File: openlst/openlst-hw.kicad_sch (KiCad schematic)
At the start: 73 parts, among them J10 Conn_01x02, J2 CC Prog/Debug, J3 UART0, J4 SPI0, J5 Control Outputs, J6 ANT, J9 Conn_01x02, U2 CC1110, U4 FOX924 27MHz, U5 TLV803S, U6 PE4259, U8 SF2446E, U9 RFFM6406

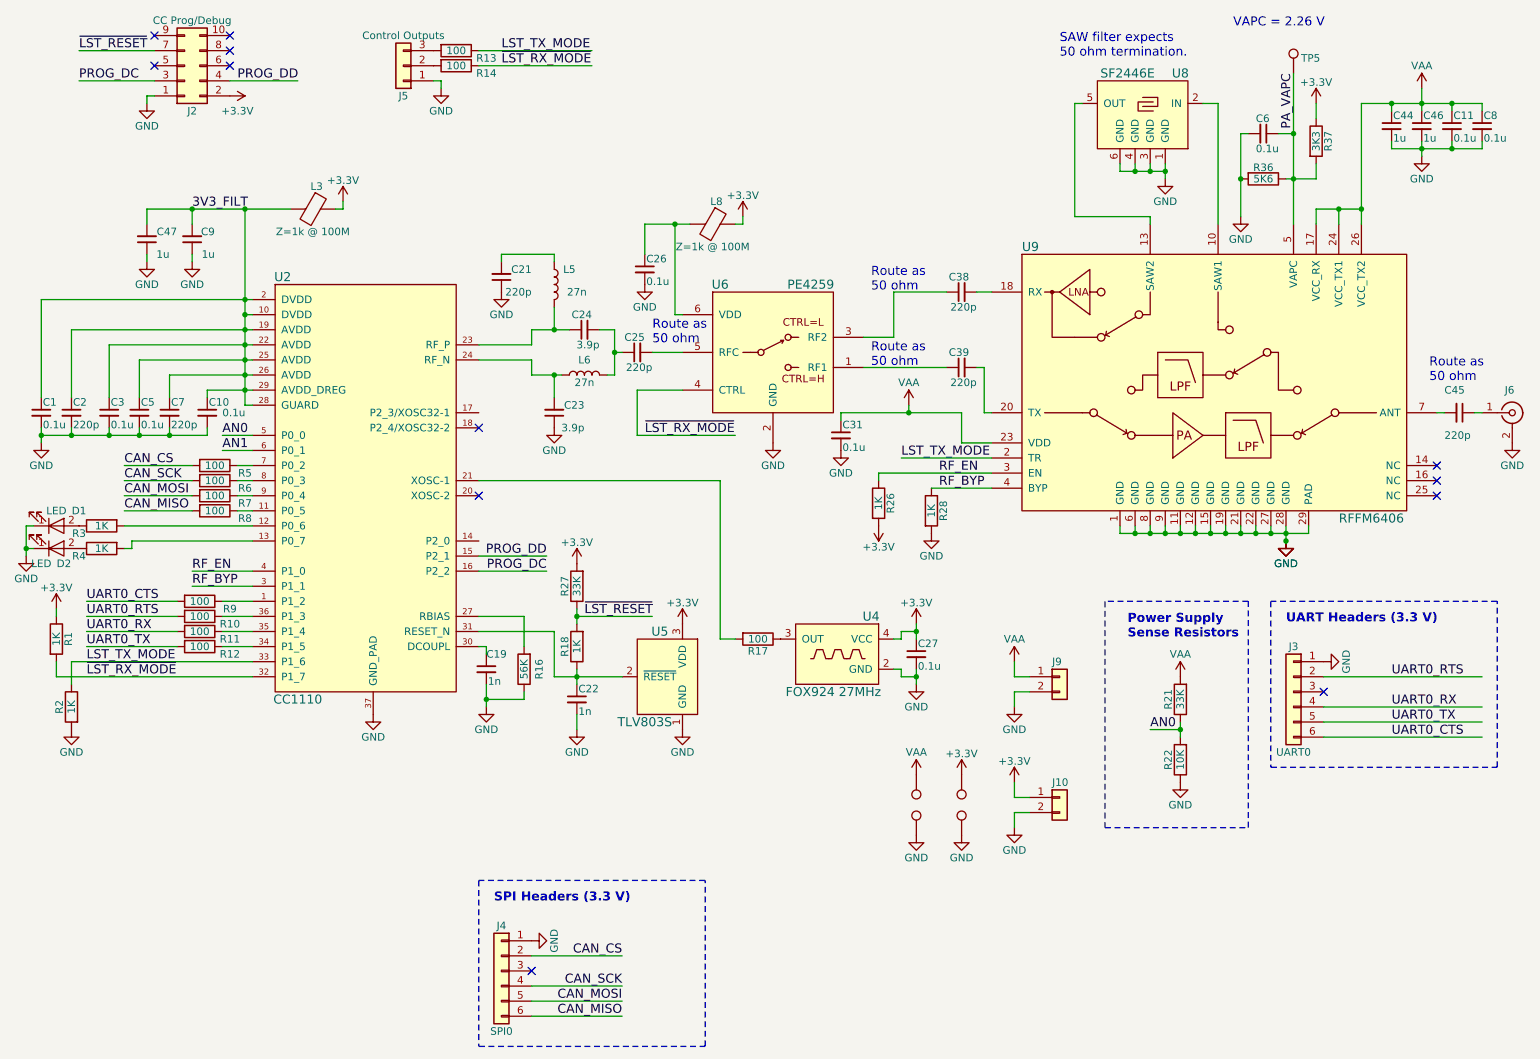
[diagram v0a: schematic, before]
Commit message: Finished schematic, partially finished BOM, cleaned up old files
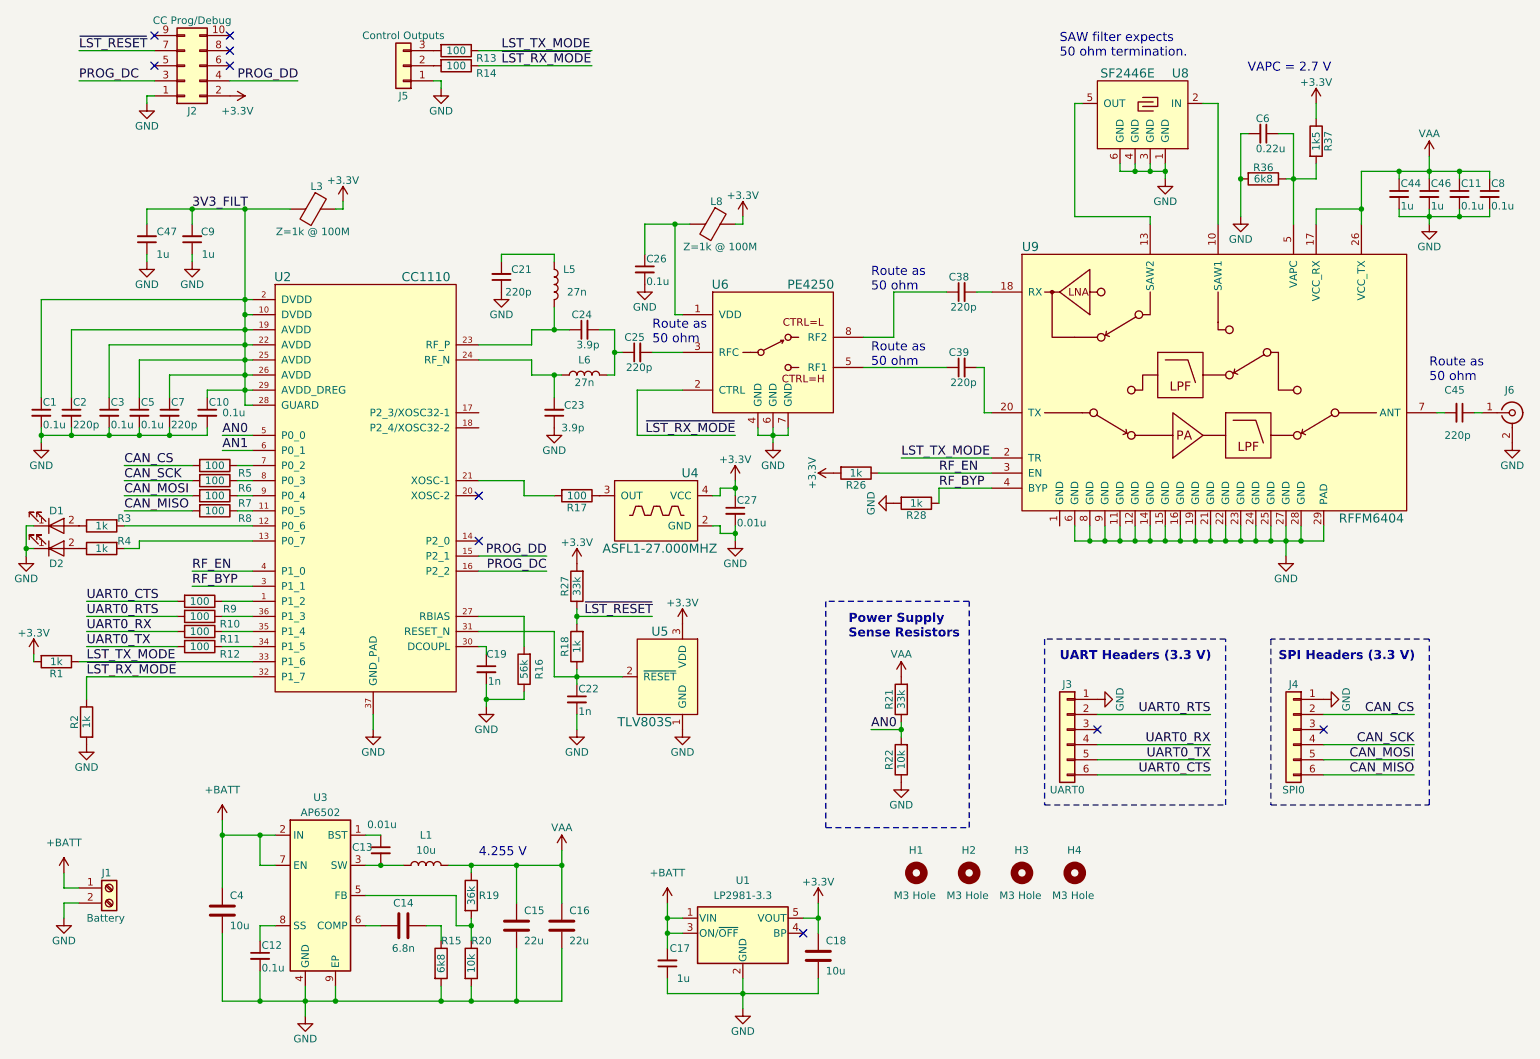
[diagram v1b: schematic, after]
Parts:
- removed C31: 0.1u, Capacitor_SMD:C_0603_1608Metric, symbol openlst-hw:C_Small
- removed J10, J9: Conn_01x02, Connector_PinHeader_2.54mm:PinHeader_1x02_P2.54mm_Vertical, symbol Connector_Generic:Conn_01x02
- removed TP1, TP2, TP3, TP4: TestPoint, TestPoint:TestPoint_Keystone_5010-5014_Multipurpose, symbol Connector:TestPoint
- removed TP5: TestPoint, TestPoint:TestPoint_Pad_D1.0mm, symbol Connector:TestPoint
- removed U6: PE4259, Package_TO_SOT_SMD:SOT-363_SC-70-6, symbol openlst-hw:PE4259
- removed U9: RFFM6406, openlst:Qorvo_LGA_28_ThermalVias, symbol openlst-hw:RFFM6406
- added C12: 0.1u, Capacitor_SMD:C_0603_1608Metric, symbol openlst-hw:C_Small
- added C13: 0.01u, Capacitor_SMD:C_0603_1608Metric, symbol openlst-hw:C_Small
- added C14: 6.8n, Capacitor_SMD:C_0603_1608Metric, symbol Device:C
- added C15, C16: 22u, symbol Device:C
- added C17: 1u, Capacitor_SMD:C_0603_1608Metric, symbol openlst-hw:C_Small
- added C18: 10u, Capacitor_SMD:C_0603_1608Metric, symbol Device:C
- added C4: 10u, Capacitor_SMD:C_0805_2012Metric, symbol Device:C
- added H1, H2, H3, H4: M3 Hole, MountingHole:MountingHole_3.2mm_M3, symbol Mechanical:MountingHole
- added J1: Battery, symbol Connector:Screw_Terminal_01x02
- added L1: 10u, Inductor_SMD:L_Vishay_IFSC-1515AH_4x4x1.8mm, symbol Device:L
- added R15: 6k8, Resistor_SMD:R_0603_1608Metric, symbol Device:R
- added R19: 36k, Resistor_SMD:R_0603_1608Metric, symbol Device:R
- added R20: 10k, Resistor_SMD:R_0603_1608Metric, symbol Device:R
- added U1: LP2981-3.3, Package_TO_SOT_SMD:SOT-23-5, symbol Regulator_Linear:LP2985-3.3
- added U3: AP6502, Package_SO:SOIC-8-1EP_3.9x4.9mm_P1.27mm_EP2.62x3.51mm_ThermalVias, symbol Regulator_Switching:AP6502
- added U6: PE4250, Package_SO:MSOP-8_3x3mm_P0.65mm, symbol openlst-hw:PE4250
- added U9: RFFM6404, openlst:Qorvo_LGA_28_ThermalVias, symbol openlst-hw:RFFM6404
- C1, C10, C11, C26, C3, C5, C8: Manuf AVX -> (none); ManufPN 0603YC104K4T4A -> (none); Supplier Digikey -> (none); SupplierPN 478-9382-1-ND -> (none)
- C19, C22: Manuf Murata -> (none); ManufPN GCM188R71E102KA37D -> (none); Supplier Digikey -> (none); SupplierPN 490-8016-1-ND -> (none)
- C2, C21, C25, C38, C39, C45, C7: Manuf Kemet -> (none); ManufPN C0402C221J2GACAUTO -> (none); Supplier Digikey -> (none); SupplierPN 399-11552-1-ND -> (none)
- C23, C24: Manuf Murata -> (none); ManufPN GJM1555C1H3R9CB01D -> (none); Supplier Digikey -> (none); SupplierPN 490-3097-1-ND -> (none)
- C27: value 0.1u -> 0.01u; Manuf AVX -> (none); ManufPN 0603YC104K4T4A -> (none); Supplier Digikey -> (none); SupplierPN 478-9382-1-ND -> (none)
- C44, C46, C47, C9: Manuf Samsung -> (none); ManufPN CL10B105MO8NNWC -> (none); Supplier Digikey -> (none); SupplierPN 1276-6524-6-ND -> (none)
- C6: value 0.1u -> 0.22u; Manuf AVX -> (none); ManufPN 0603YC104K4T4A -> (none); Supplier Digikey -> (none); SupplierPN 478-9382-1-ND -> (none)
- D1: Manuf Wurth -> (none); ManufPN 150060VS75000 -> (none); Supplier Digikey -> (none); SupplierPN 732-4980-1-ND -> (none)
- D2: Manuf Wurth -> (none); ManufPN 150060SS75000 -> (none); Supplier Digikey -> (none); SupplierPN 732-4979-1-ND -> (none)
- J2: Manuf Samtec -> (none); ManufPN FTSH-105-01-L-DV-K-P -> (none); Supplier Digikey -> (none); SupplierPN SAM9076-ND -> (none)
- J3, J4: Manuf Wurth -> (none); ManufPN 61300611121 -> (none); Supplier Digikey -> (none); SupplierPN 732-5319-ND -> (none)
- L3, L8: Manuf Wurth -> Pulse Electronics Network; ManufPN 74279266 -> PE-0603FB102ST; SupplierPN 732-4484-1-ND -> 553-2381-1-ND
- L5, L6: Manuf Murata -> (none); ManufPN LQW15AN27NJ00D -> (none); Supplier Digikey -> (none); SupplierPN 490-1151-1-ND -> (none)
- R1, R18, R2, R26, R28, R3, R4: value 1K -> 1k; Manuf Yageo -> (none); ManufPN RC0603JR-071KL -> (none); Supplier Digikey -> (none); SupplierPN 311-1.0KGRCT-ND -> (none)
- R10, R11, R12, R13, R14, R17, R5, R6, R7, R8, R9: Manuf Yageo -> (none); ManufPN AC0603FR-07100RL -> (none); Supplier Digikey -> (none); SupplierPN YAG3561CT-ND -> (none)
- R16: value 56K -> 56k; Manuf Stackpole -> (none); ManufPN RMCF0603FT56K0 -> (none); Supplier Digikey -> (none); SupplierPN RMCF0603FT56K0CT-ND -> (none)
- R21, R27: value 33K -> 33k; Manuf Yageo -> (none); ManufPN AC0603FR-0733KL -> (none); Supplier Digikey -> (none); SupplierPN YAG3598CT-ND -> (none)
- R22: value 10K -> 10k; Manuf Yageo -> (none); ManufPN RC0603JR-0710KL -> (none); Supplier Digikey -> (none); SupplierPN 311-10KGRCT-ND -> (none)
- R36: value 5K6 -> 6k8; Manuf Stackpole -> (none); ManufPN RMCF0603FT5K60 -> (none); Supplier Digikey -> (none); SupplierPN RMCF0603FT5K60CT-ND -> (none)
- R37: value 3K3 -> 1k5; Manuf Stackpole -> (none); ManufPN RMCF0603FT3K30 -> (none); Supplier Digikey -> (none); SupplierPN RMCF0603FT3K30CT-ND -> (none)
- U2: Supplier Digikey -> Texas Instruments; SupplierPN 296-38560-1-ND -> CC1110F32RHHR
- U4: value FOX924 27MHz -> ASFL1-27.000MHZ; footprint Oscillator:Oscillator_SMD_Fordahl_DFAS15-4Pin_5.0x3.2mm -> Oscillator:Oscillator_SMD_SeikoEpson_SG8002LB-4Pin_5.0x3.2mm; Manuf Fox Electronics -> Abracon; ManufPN FT5HNBPK27.0-T1 -> ASFL1-27.000MHZ-EK-T; SupplierPN 631-1075-1-ND -> 535-9263-1-ND
- U8: Manuf (none) -> RFMi; ManufPN (none) -> SF2446E; Supplier (none) -> Digikey Marketplace; SupplierPN (none) -> 2410-SF2446E-ND
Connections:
- net +3V3: now also R1.2, C18.1, U1.5 (VOUT); no longer R1.1
- net GND: now also C12.2, C15.2, C16.2, C17.1, C18.2, C4.1, J1.2 (Pin_2), R15.2, R20.2, U1.2 (GND), U3.4 (GND), U3.9 (EP), U6.4 (GND), U6.6 (GND), U6.7 (GND), U9.11 (GND), U9.12 (GND), U9.14 (GND), U9.15 (GND), U9.16 (GND), U9.19 (GND), U9.21 (GND), U9.22 (GND), U9.23 (GND), U9.24 (GND), U9.25 (GND), U9.27 (GND), U9.28 (GND), U9.29 (PAD), U9.6 (GND), U9.8 (GND), U9.9 (GND)
- net LST_TX_MODE: now also R1.1, U9.2 (TR); no longer R2.1
- net RF_BYP: now also U9.4 (BYP)
- net RF_EN: now also U9.3 (EN)
- net VAA: now also C15.1, C16.1, L1.2, R19.1, U9.17 (VCC_RX), U9.26 (VCC_TX)
- net at C45.2: now also U9.7 (ANT)
- net at C25.2: now also U6.3 (RFC)
- net at C39.1: now also U6.5 (RF1)
- net at C38.1: now also U6.8 (RF2)
- net at C26.1, L8.2: now also U6.1 (VDD)
- net at C38.2: now also U9.18 (RX)
- net at C39.2: now also U9.20 (TX)
- net at U8.2 (IN): now also U9.10 (SAW1)
- net at U8.5 (OUT): now also U9.13 (SAW2)
- net PA_VAPC: no longer names the net of C6.1, R36.1, R37.2
- net PA_VAPC: now also U9.5 (VAPC)
- net ~LST_RESET renamed ~{LST_RESET}
- net ~LST_RX_MODE renamed ~{LST_RX_MODE}
- net ~{LST_RX_MODE}: now also R2.1, U6.2 (CTRL); no longer R1.2
- new net: C14.1, U3.6 (COMP)
- new net: C14.2, R15.1
- new net: R19.2, R20.1, U3.5 (FB)
- new net: C13.1, U3.1 (BST)
- new net: C13.2, L1.1, U3.3 (SW)
- new net: C12.1, U3.8 (SS)
- new net +BATT: C17.2, C4.2, J1.1 (Pin_1), U1.1 (VIN), U1.3 (ON/~{OFF}), U3.2 (IN), U3.7 (EN)
- no-connect marks 12 -> 10
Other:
- note added: "4.255 V"
- note added: "VAPC = 2.7 V"
- note removed: "VAPC = 2.26 V"
- moved on the sheet: C11, C27, C44, C46, C8, J3, J4, R1, R17, R2, R21, R22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

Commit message: Updated BOM
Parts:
- removed C17: 1u, Capacitor_SMD:C_0603_1608Metric, symbol openlst-hw:C_Small
- added C17: 10u, Capacitor_SMD:C_0805_2012Metric, symbol Device:C
- C1, C10, C11, C12, C26, C3, C5, C8: Manuf (none) -> Samsung; ManufPN (none) -> CL10B104MB8NNNC; Supplier (none) -> Digikey; SupplierPN (none) -> 1276-1941-1-ND
- C13, C27: Manuf (none) -> Murata; ManufPN (none) -> GCM188R72A103KA37D; Supplier (none) -> Digikey; SupplierPN (none) -> 490-4781-1-ND
- C14: Manuf (none) -> KEMET; ManufPN (none) -> C0603C682K5RACTU; Supplier (none) -> Digikey; SupplierPN (none) -> 399-1089-1-ND
- C15, C16: footprint (none) -> Capacitor_SMD:C_1210_3225Metric; Manuf (none) -> TDK; ManufPN (none) -> C3225X7R1C226M250AC; Supplier (none) -> Digikey; SupplierPN (none) -> 445-3955-1-ND
- C18: footprint Capacitor_SMD:C_0603_1608Metric -> Capacitor_SMD:C_0805_2012Metric; Manuf (none) -> Taiyo Yuden; ManufPN (none) -> GMK316AB7106KL-TR; Supplier (none) -> Digikey; SupplierPN (none) -> 587-3007-1-ND
- C19, C22: Manuf (none) -> AVX; ManufPN (none) -> 06035C102KAT2A; Supplier (none) -> Digikey; SupplierPN (none) -> 478-1215-1-ND
- C2, C21, C25, C38, C39, C45, C7: Manuf (none) -> Murata; ManufPN (none) -> GCM1555C1H221JA16D; Supplier (none) -> Digikey; SupplierPN (none) -> 490-4927-1-ND
- C23, C24: Manuf (none) -> Samsung; ManufPN (none) -> CL05C3R9CB5NNNC; Supplier (none) -> Digikey; SupplierPN (none) -> 1276-1695-1-ND
- C4: Manuf (none) -> Taiyo Yuden; ManufPN (none) -> GMK316AB7106KL-TR; Supplier (none) -> Digikey; SupplierPN (none) -> 587-3007-1-ND
- C44, C46, C47, C9: Manuf (none) -> Samsung; ManufPN (none) -> CL10B105MO8NNWC; Supplier (none) -> Digikey; SupplierPN (none) -> 1276-6524-1-ND
- C6: Manuf (none) -> Samsung; ManufPN (none) -> CL10B224KO8NNNC; Supplier (none) -> Digikey; SupplierPN (none) -> 1276-1112-1-ND
- D1, D2: Manuf (none) -> Wurth; ManufPN (none) -> 150060VS75000; Supplier (none) -> Digikey; SupplierPN (none) -> 732-4980-1-ND
- J1: footprint (none) -> TerminalBlock_Phoenix:TerminalBlock_Phoenix_MKDS-1,5-2-5.08_1x02_P5.08mm_Horizontal; Manuf (none) -> Phoenix Contact; ManufPN (none) -> 1729128; Supplier (none) -> Digikey; SupplierPN (none) -> 277-1247-ND
- J2: Manuf (none) -> Samtec; ManufPN (none) -> FTSH-105-01-F-DV-K-TR; Supplier (none) -> Digikey; SupplierPN (none) -> SAM13160CT-ND
- J6: Manuf (none) -> Samtec; ManufPN (none) -> SMA-J-P-H-ST-EM1; Supplier (none) -> Samtec
- L5, L6: Manuf (none) -> Murata; ManufPN (none) -> LQW15AN27NJ00D; Supplier (none) -> Digikey; SupplierPN (none) -> 490-1151-1-ND
- R1, R18, R2, R26, R28, R3, R4: Manuf (none) -> Yageo; ManufPN (none) -> RC0603FR-071KL; Supplier (none) -> Digikey; SupplierPN (none) -> 311-1.00KHRCT-ND
- R10, R11, R12, R13, R14, R17, R5, R6, R7, R8, R9: Manuf (none) -> Yageo; ManufPN (none) -> RC0603FR-07100RL; Supplier (none) -> Digikey; SupplierPN (none) -> 311-100HRCT-ND
- R15, R36: Manuf (none) -> Yageo; ManufPN (none) -> RC0603FR-076K8L; Supplier (none) -> Digkey; SupplierPN (none) -> 311-6.80KHRCT-ND
- R16: Manuf (none) -> Yageo; ManufPN (none) -> RC0603FR-0756KL; Supplier (none) -> Digikey; SupplierPN (none) -> 311-56KHRCT-ND
- R19: Manuf (none) -> Yageo; ManufPN (none) -> RC0603FR-0736KL; Supplier (none) -> Digikey; SupplierPN (none) -> 311-36.0KHRCT-ND
- R20, R22: Manuf (none) -> Yageo; ManufPN (none) -> RC0603FR-0710KL; Supplier (none) -> Digikey; SupplierPN (none) -> 311-10.0KHRCT-ND
- R21, R27: Manuf (none) -> Stackpole Electronics; ManufPN (none) -> RMCF0603FT33K0; Supplier (none) -> Digikey; SupplierPN (none) -> RMCF0603FT33K0CT-ND
- R37: Manuf (none) -> Panasonic; ManufPN (none) -> ERJ-3EKF1501V; Supplier (none) -> Digikey; SupplierPN (none) -> P1.50KHCT-ND
- U5: value TLV803S -> APX803S00; Manuf Texas Instruments -> Diodes Inc; ManufPN TLV803SDBZR -> APX803S00-29SR-7; SupplierPN 296-29196-1-ND -> APX803S00-29SR-7DICT-ND
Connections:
- net +BATT: now also C17.2
- net GND: now also U9.1 (GND), C17.1
